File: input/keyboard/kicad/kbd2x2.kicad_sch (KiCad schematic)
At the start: 8 parts, among them SW1 mykbd, SW2 mykbd, SW3 mykbd, SW4 mykbd

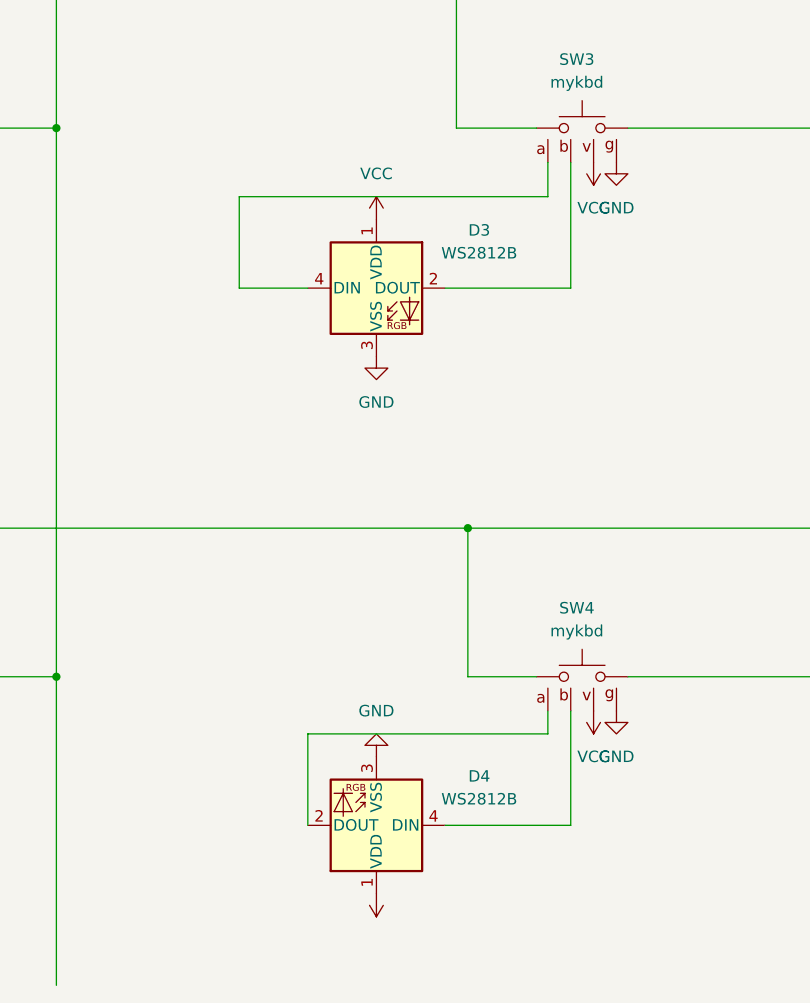
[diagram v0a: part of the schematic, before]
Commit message: reorganize dir, keyboard pcb update
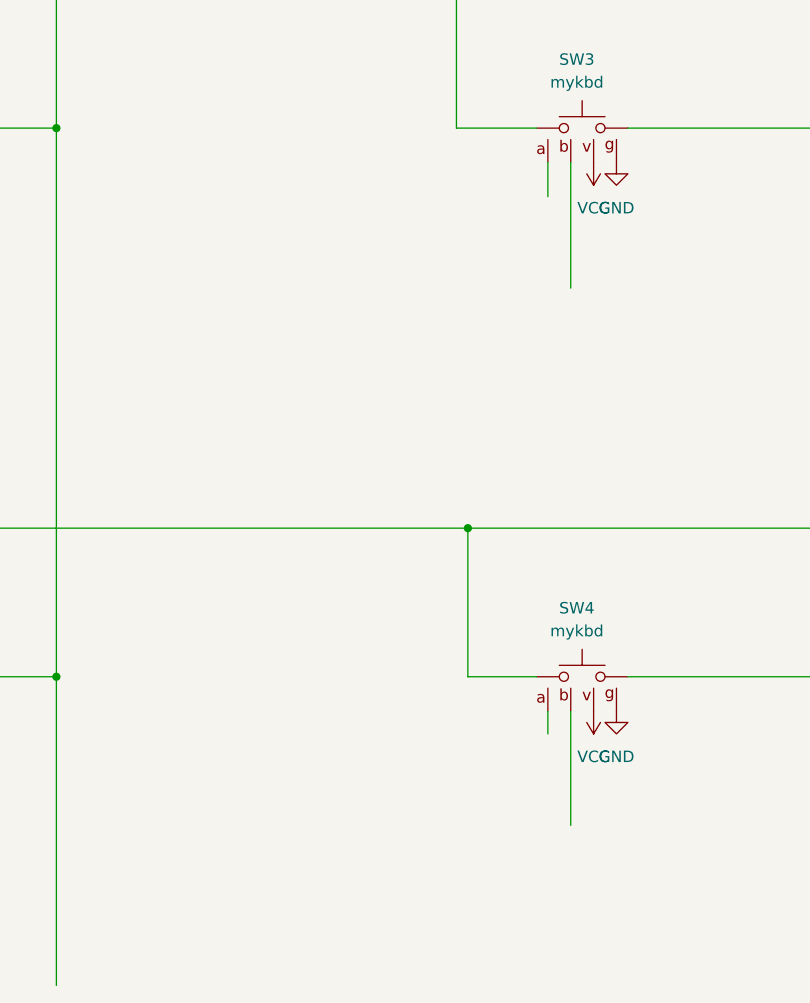
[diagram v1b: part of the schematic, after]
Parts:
- removed D3, D4: WS2812B, LED_SMD:LED_WS2812B_PLCC4_5.0x5.0mm_P3.2mm, symbol LED:WS2812B
- SW4: footprint mykbd:seat -> mykbd:seat_b
